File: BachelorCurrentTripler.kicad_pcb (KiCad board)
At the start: 4 copper layers, 153.3 x 77.8 mm, 74 parts, among them J1 Conn_01x07_Pin, J2 Conn_01x01_Pin, J3 Conn_01x01_Pin, J5 Conn_01x01_Pin, J6 Conn_01x01_Pin, J7 Conn_01x01_Pin, Q10 IRLR8726EBF, Q11 IRLR8726EBF, Q13 C2M0025120D, Q14 C2M0025120D, Q15 C2M0025120D, Q16 C2M0025120D, Q7 C2M0025120D, Q8 C2M0025120D, Q9 IRLR8726EBF, U1 STDriveG600, U2 STDriveG600, U3 STDriveG600, U4 FAN3268, U5 FAN3268, U6 FAN3268

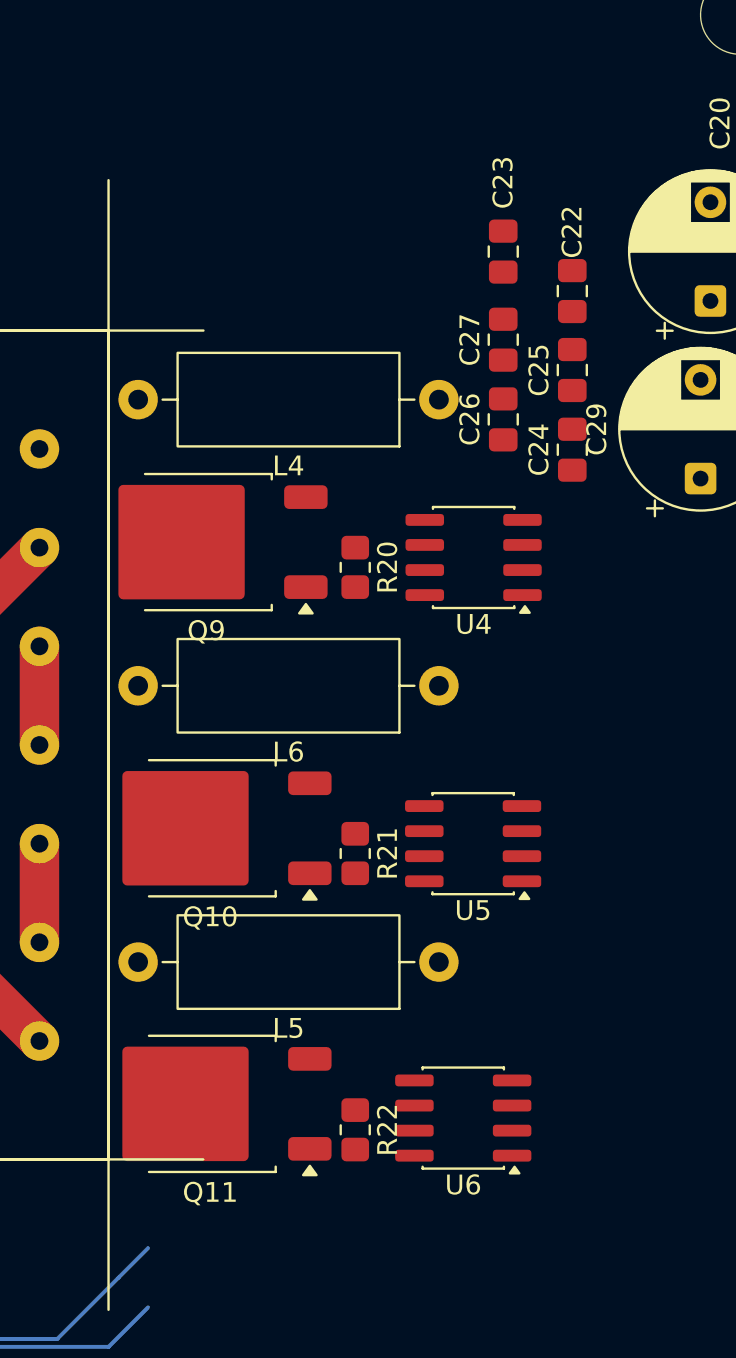
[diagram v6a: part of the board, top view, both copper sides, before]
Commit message: Added Decoupling and some tracing
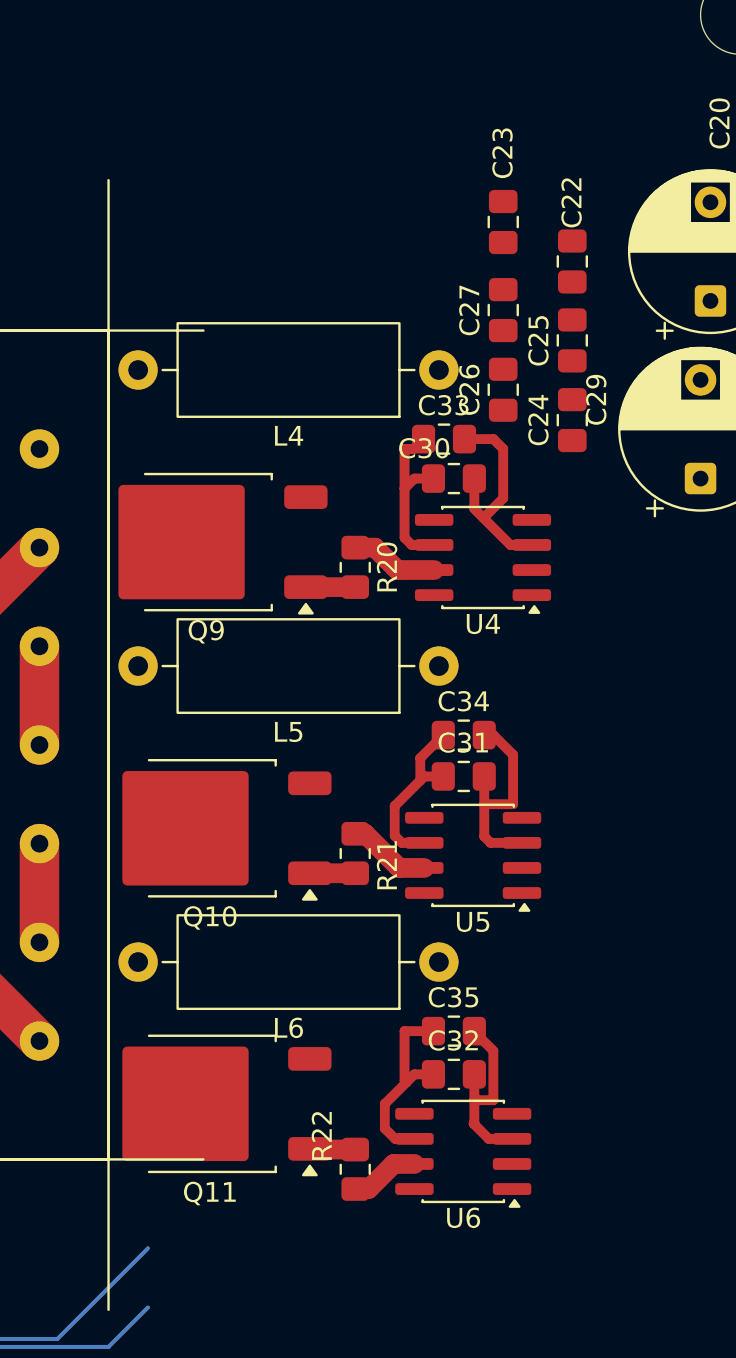
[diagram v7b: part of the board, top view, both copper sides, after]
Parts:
- added C30: 100n, Capacitor_SMD:C_0805_2012Metric_Pad1.18x1.45mm_HandSolder, F.Cu at (206.5, 92.5)
- added C31: 100n, Capacitor_SMD:C_0805_2012Metric_Pad1.18x1.45mm_HandSolder, F.Cu at (207.0, 107.6)
- added C32: 100n, Capacitor_SMD:C_0805_2012Metric_Pad1.18x1.45mm_HandSolder, F.Cu at (206.5, 122.7)
- added C33: 1u, Capacitor_SMD:C_0805_2012Metric_Pad1.18x1.45mm_HandSolder, F.Cu at (206.0, 90.5)
- added C34: 1u, Capacitor_SMD:C_0805_2012Metric_Pad1.18x1.45mm_HandSolder, F.Cu at (207.0, 105.5)
- added C35: 1u, Capacitor_SMD:C_0805_2012Metric_Pad1.18x1.45mm_HandSolder, F.Cu at (206.5, 120.5)
- R20, R21, R22: value 5m -> R
- moved L5 15.0 mm to (205.7, 102.0)
- moved L6 14.0 mm to (205.7, 117.0)
- moved R22 2.00 mm to (201.5, 127.5), turned to 90 degrees
- moved U6 1.69 mm to (207.0, 126.6)
- moved C22 1.50 mm to (212.5, 81.5)
- moved C23 1.50 mm to (209.0, 79.5)
- moved C24 1.50 mm to (212.5, 89.5)
- moved C25 1.50 mm to (212.5, 85.5)
- moved C26 1.50 mm to (209.0, 88.0)
- moved C27 1.50 mm to (209.0, 84.0)
- moved L4 1.50 mm to (205.7, 87.0)
- moved U5 0.59 mm to (207.5, 111.6)
- moved U4 0.47 mm to (208.0, 96.5)
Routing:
- net GND: track 22.0 -> 53.8 mm
- net +12V: track 153.4 -> 181.5 mm
- net Net-(U4-OUTA): track 0.00 -> 4.47 mm
- net Net-(U5-OUTA): track 0.00 -> 4.22 mm
- net Net-(U6-OUTA): track 0.00 -> 3.53 mm
- net Net-(Q9-G): track 0.00 -> 2.50 mm
- net Net-(Q11-G): track 0.00 -> 2.31 mm
- net Net-(Q10-G): track 0.00 -> 2.30 mm

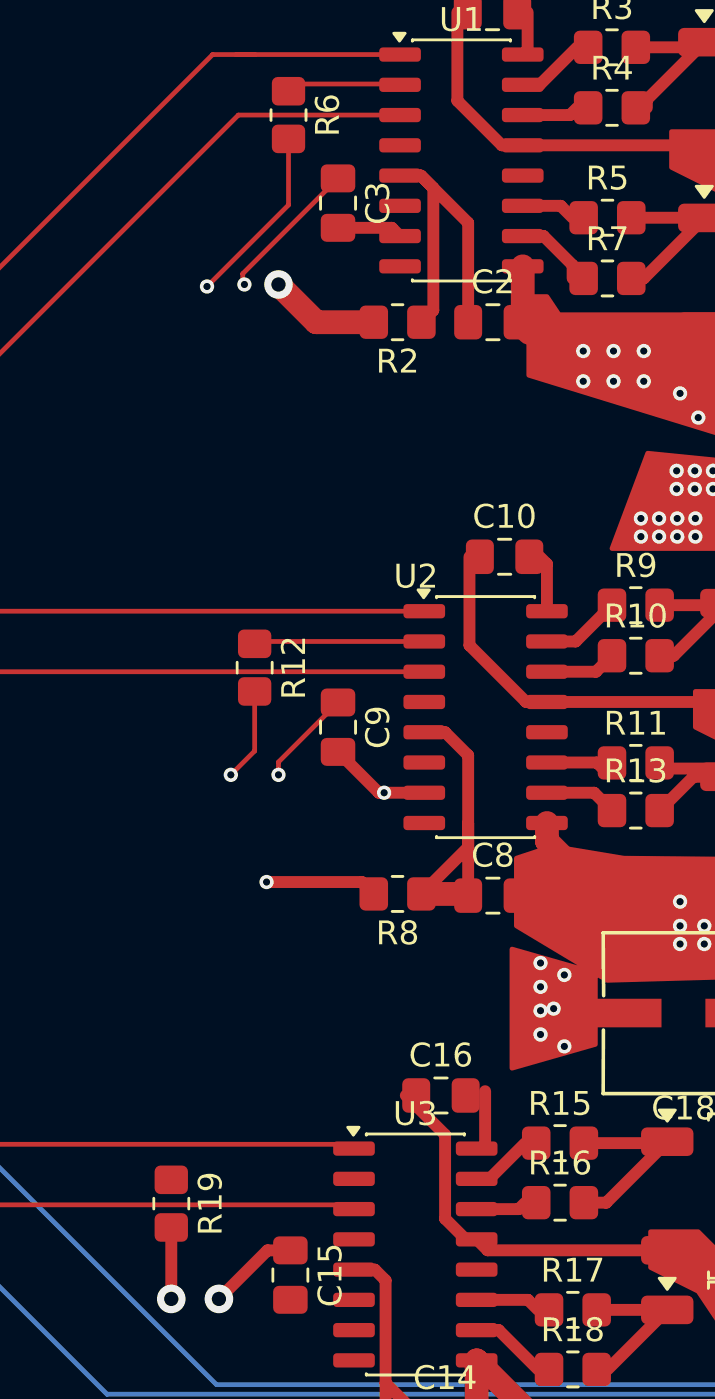
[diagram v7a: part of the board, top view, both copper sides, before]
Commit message: Added Connections to primary side
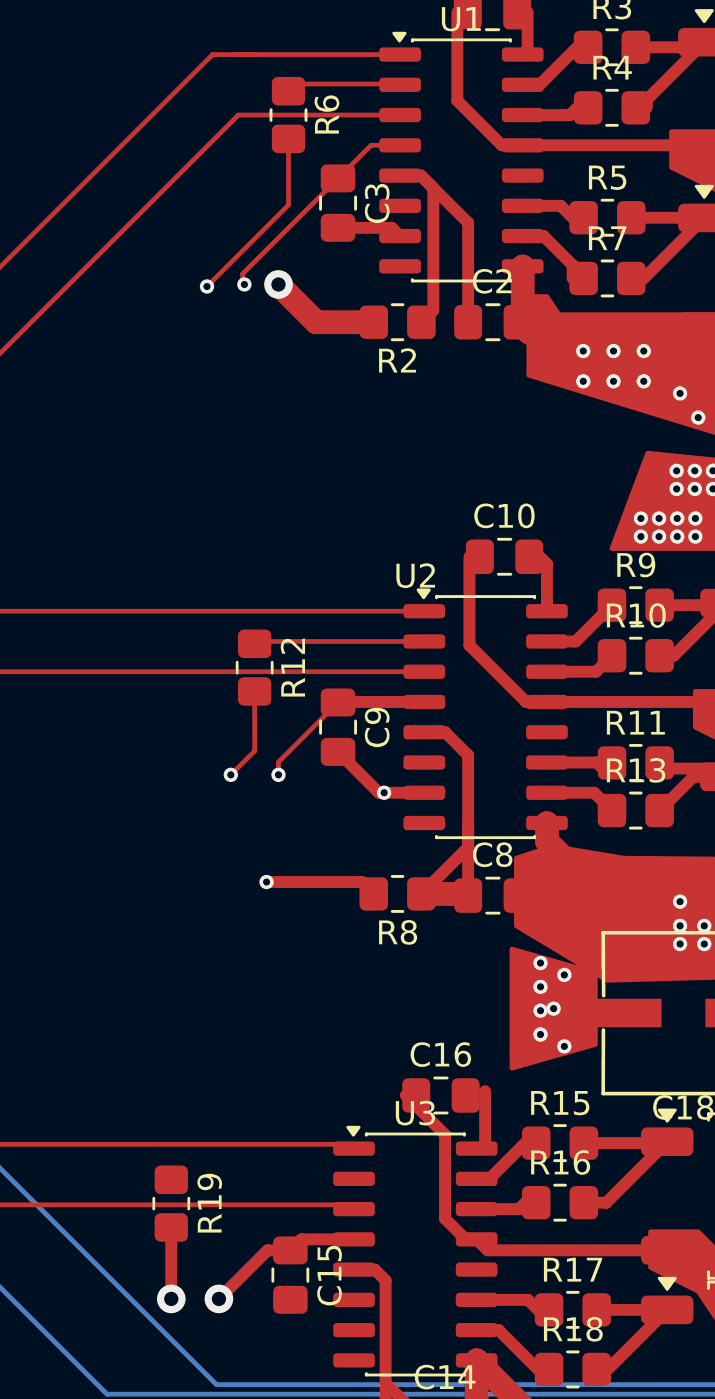
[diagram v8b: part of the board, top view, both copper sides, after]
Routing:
- net +12V: track 181.5 -> 191.2 mm
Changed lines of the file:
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@@
+	)
+	(segment
+		(start 123.0995 107.4625)
+		(end 123.12 107.442)
+		(width 0.2)
+		(layer "F.Cu")
+		(net 3)
 	)
 	(segment
@@
 		(end 204 95.5)
 		(width 0.5)
+		(layer "F.Cu")
+		(net 3)
+	)
+	(segment
+		(start 120.8885 84.074)
+		(end 122.104 84.074)
+		(width 0.2)
 		(layer "F.Cu")
 		(net 3)
@@
 	)
 	(segment
+		(start 119.5205 107.442)
+		(end 119.5 107.4625)
+		(width 0.2)
+		(layer "F.Cu")
+		(net 3)
+	)
+	(segment
 		(start 204.5 122.69)
 		(end 205.4625 122.69)
@@
 	)
 	(segment
+		(start 123.12 107.442)
+		(end 119.5205 107.442)
+		(width 0.5)
+		(layer "F.Cu")
+		(net 3)
+	)
+	(segment
 		(start 204 123)
 		(end 204 120.5)
@@
 	)
 	(segment
+		(start 119.5 85.4625)
+		(end 120.8885 84.074)
+		(width 0.2)
+		(layer "F.Cu")
+		(net 3)
+	)
+	(segment
+		(start 117.9625 130)
+		(end 120.17 130)
+		(width 0.5)
+		(layer "F.Cu")
+		(net 3)
+	)
+	(segment
 		(start 204 93)
 		(end 204.5 92.5)
 		(width 0.5)
 		(layer "F.Cu")
+		(net 3)
+	)
+	(segment
+		(start 117.5 130.4625)
+		(end 117.9625 130)
+		(width 0.5)
+		(layer "F.Cu")
